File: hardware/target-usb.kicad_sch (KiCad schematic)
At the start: 23 parts, among them IC3 MAX9032AKA+T, IC4 USB3343, IC5 MAX9032AKA+T, IC6 DSC6101CI2A-026.0000, IC7 MAX9032AKA+T

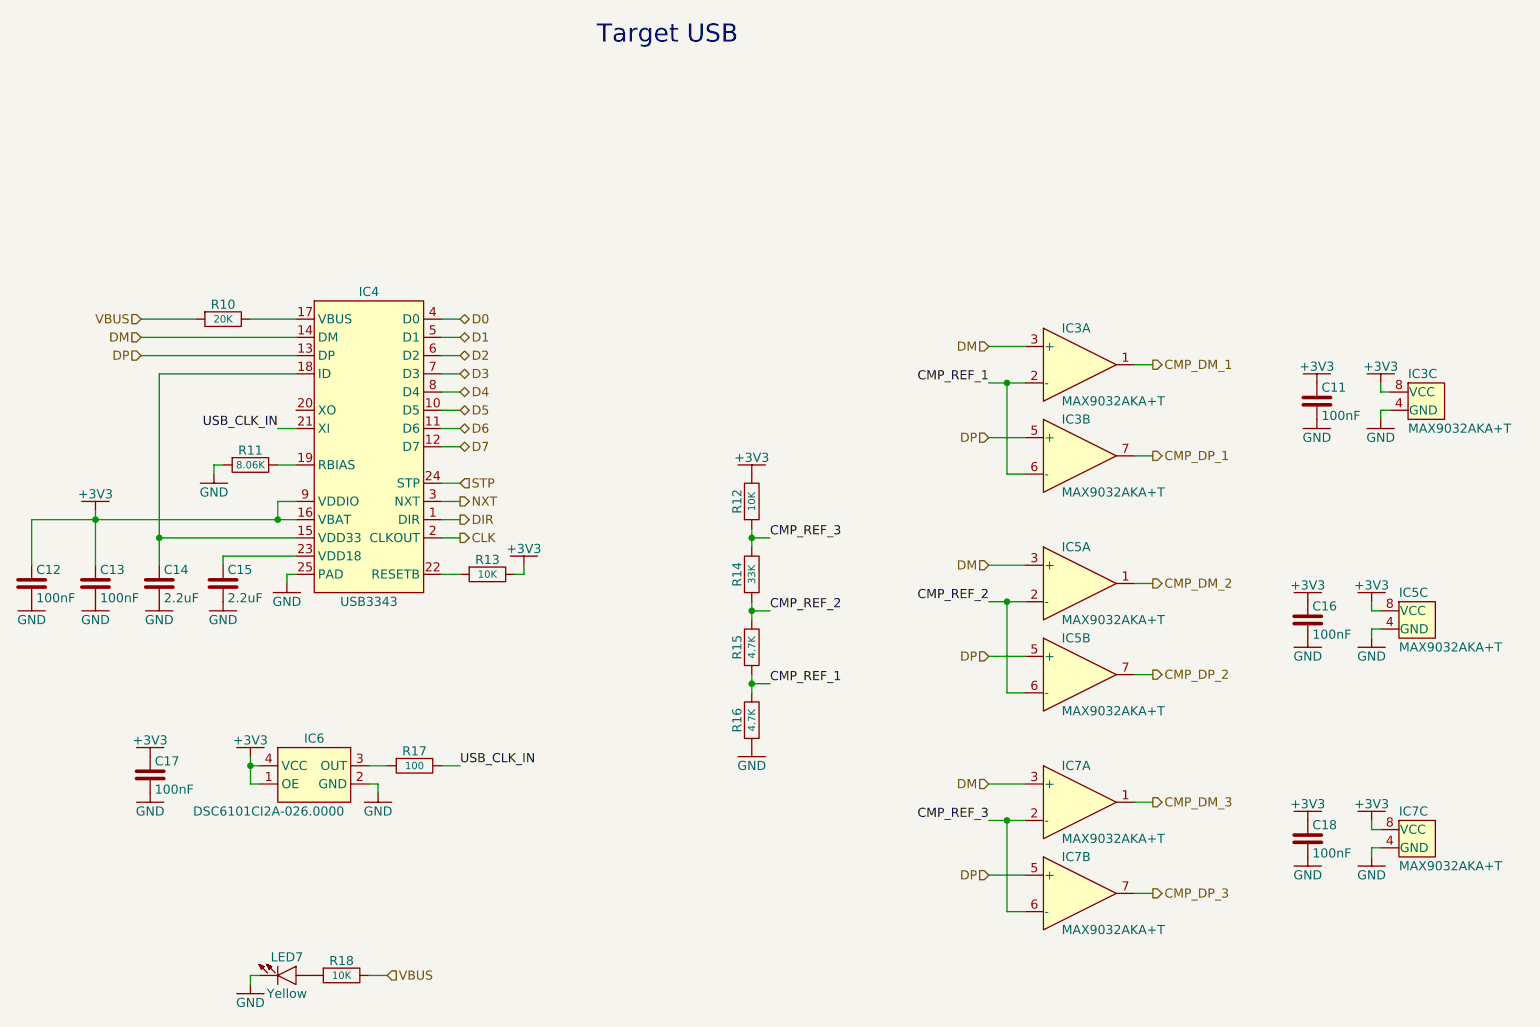
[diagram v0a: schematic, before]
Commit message: Use a single large sheet for the schematic
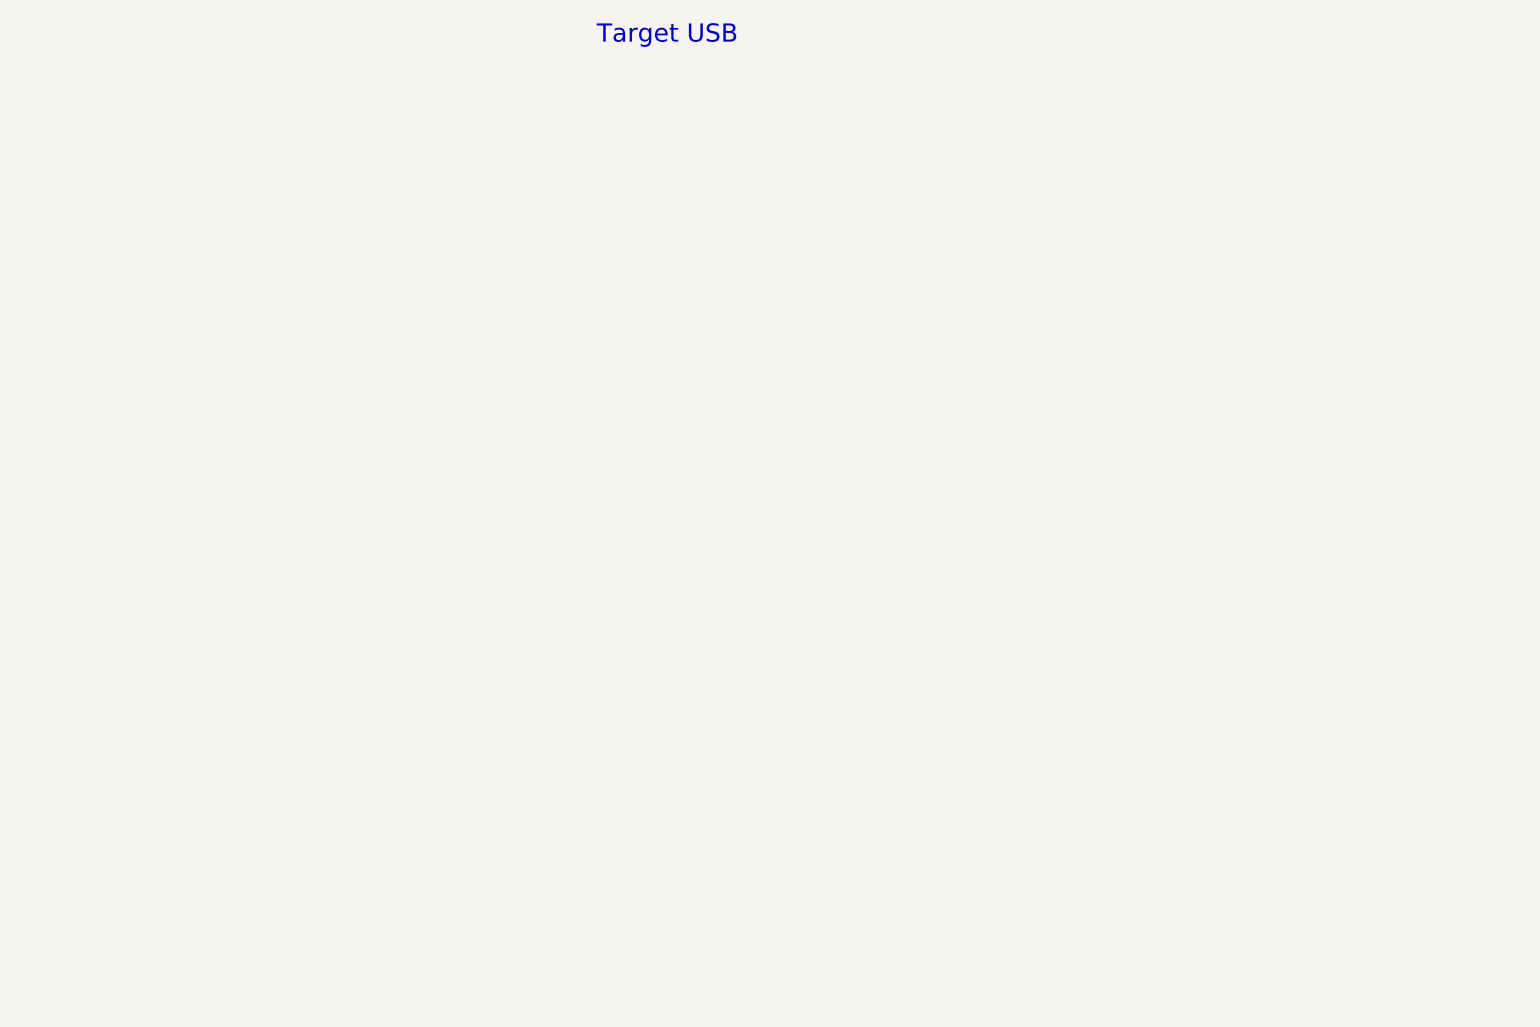
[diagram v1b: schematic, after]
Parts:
- removed C11, C12, C13, C16, C17, C18: 100nF, ataradov_smd:0603, symbol ataradov_rlc:C
- removed C14, C15: 2.2uF, ataradov_smd:0603, symbol ataradov_rlc:C
- removed IC3, IC5, IC7: MAX9032AKA+T, ataradov_ic:SOT-23-8, symbol ataradov_ic:Comp-Dual
- removed IC4: USB3343, ataradov_ic:QFN-24-0.5mm, symbol ataradov_ic:USB3343
- removed IC6: DSC6101CI2A-026.0000, ataradov_ic:CDFN-4-3.2x2.5mm, symbol ataradov_crystal:DSC61XX-MHz
- removed LED7: Yellow, ataradov_smd:0603, symbol ataradov_led:LED
- removed R10: 20K, ataradov_smd:0603, symbol ataradov_rlc:R
- removed R11: 8.06K, ataradov_smd:0603, symbol ataradov_rlc:R
- removed R12, R13, R18: 10K, ataradov_smd:0603, symbol ataradov_rlc:R
- removed R14: 33K, ataradov_smd:0603, symbol ataradov_rlc:R
- removed R15, R16: 4.7K, ataradov_smd:0603, symbol ataradov_rlc:R
- removed R17: 100, ataradov_smd:0603, symbol ataradov_rlc:R
